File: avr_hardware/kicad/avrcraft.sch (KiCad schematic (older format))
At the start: 43 parts, among them J1 AVRISP6, P1 CONN_10, T1 S553-5999-52, U1 ATMEGA328-A_CHIPACCURATE, U2 MCP1824, U3 ENC424J600, U4 A4447SLJTR, X1 CRYSTAL, X2 25MHz

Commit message: yay added newer design
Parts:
- removed X1: CRYSTAL, XTAL4P, symbol CRYSTAL
- removed X2: 25MHz, XTAL4P, symbol CRYSTAL
- added C15: 100u, PanasonicD8Cap, symbol CAPAPOL
- added C16: .1u, SM0603, symbol C
- added P2, P3, P4, P5, P6, P7, P8: CONN_1, .1SMTPIN, symbol CONN_1
- added Q1: MOSFET_P, SOT23GDS, symbol MOSFET_P
- added X1: XTAL4P, XTAL4P, symbol XTAL4P
- added X2: 25MHz, XTAL4P, symbol XTAL4P
- D3, D4: value BRIDGE-MB2S-TP -> MB2S-TP
- D5: footprint (none) -> SM0805
- P1: value CONN_10 -> ETHERNET
- R12: value 40k -> 47k
- R13: value 1.20k -> 1k
- R14: value 6.34k -> 4.7k
- U1: value ATMEGA328-A_CHIPACCURATE -> ATMEGA328
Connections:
- net labels added: POE+B
- wire segments 235 -> 271
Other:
- note added: "NOTE: 5v Rail should be roughly 4.5V"

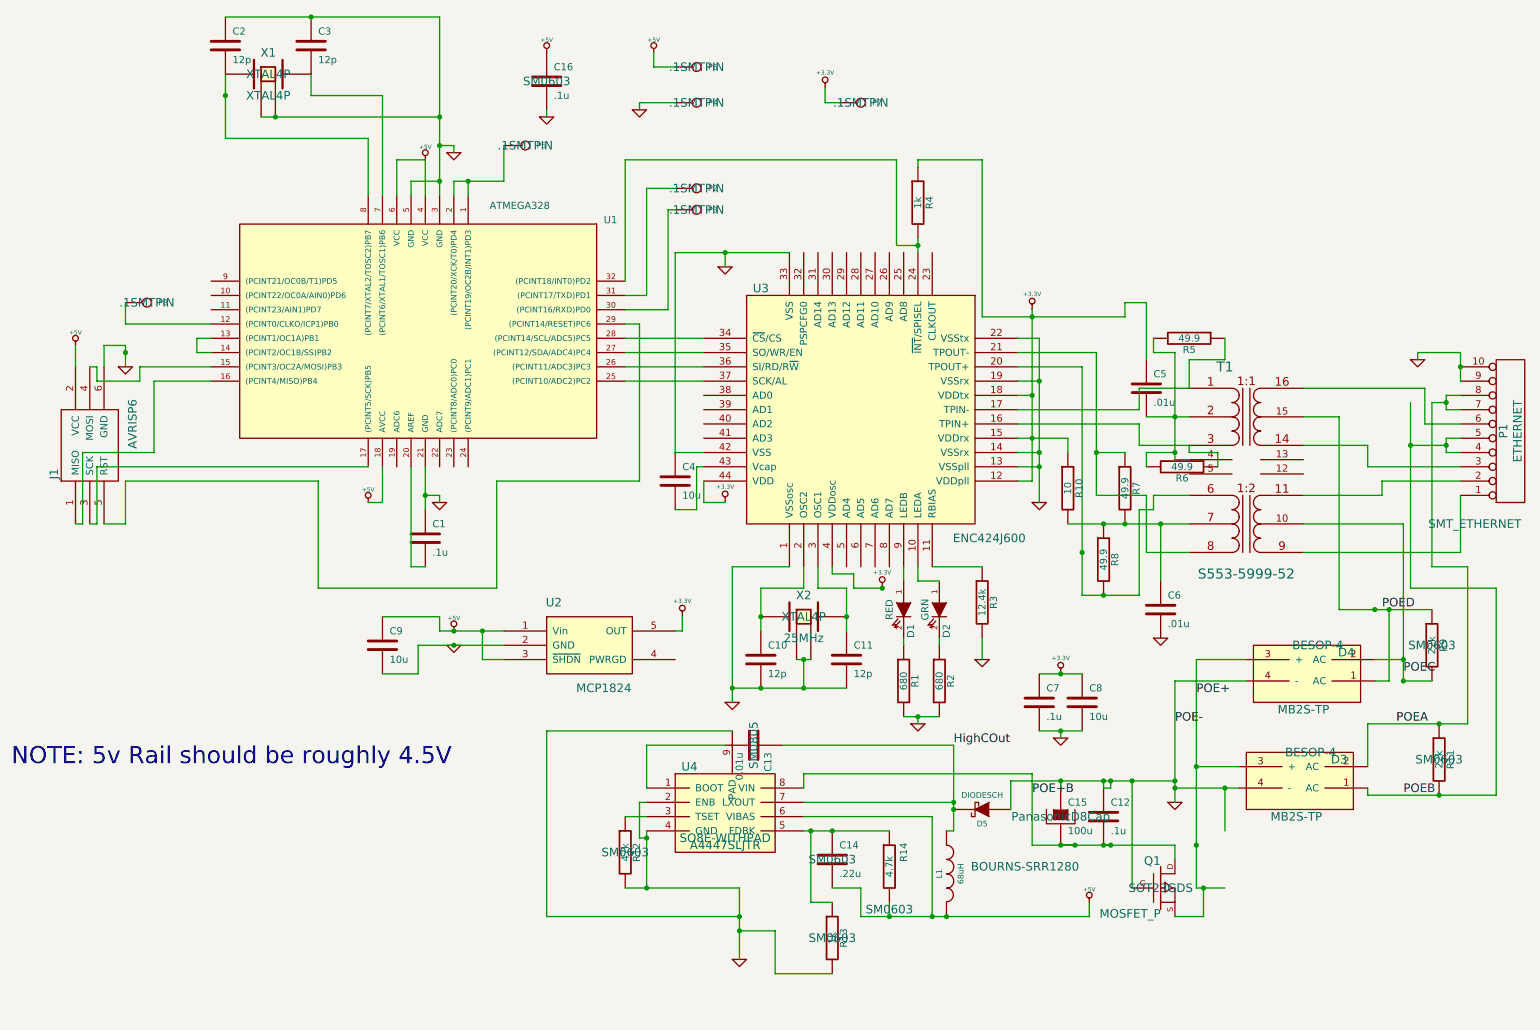
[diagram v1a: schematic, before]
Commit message: updated designs to reflect findings
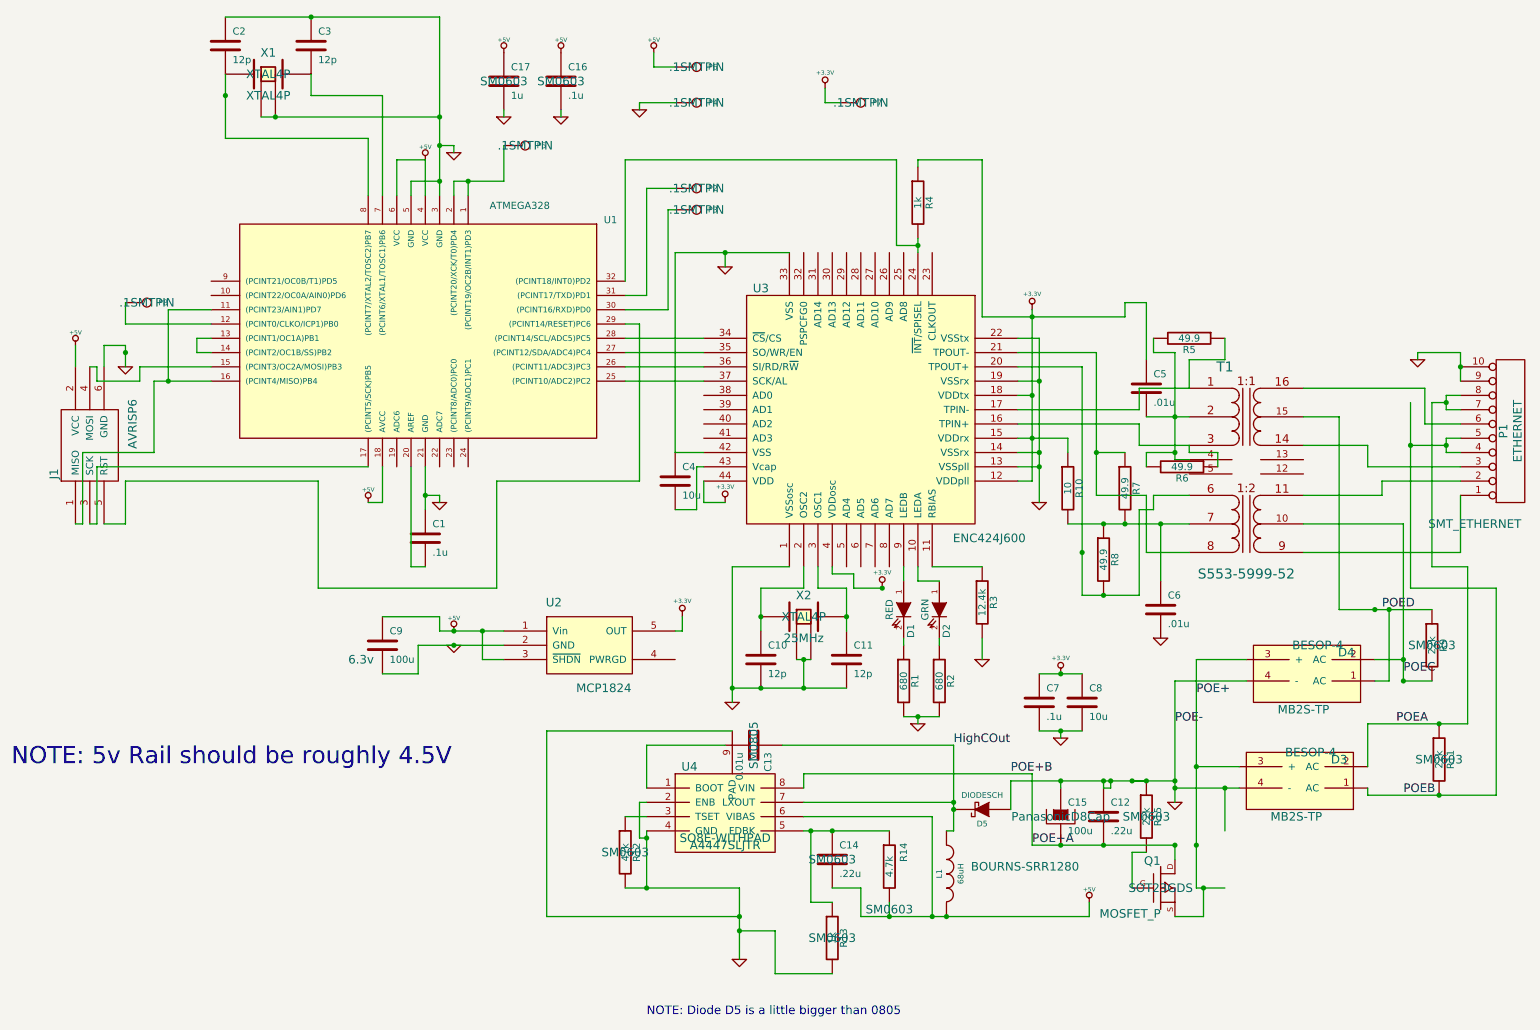
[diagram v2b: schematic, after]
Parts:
- added C17: 1u, SM0603, symbol C
- added R15: 22k, SM0603, symbol R
- C12: value .1u -> .22u
- C9: value 10u -> 100u; footprint SM0805 -> SM1206; Voltage (none) -> 6.3v
- D5: footprint SM0805 -> SM1005
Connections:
- net +5V: now also C17.1
- net GND: now also C17.2, R15.1; no longer Q1.G
- net at U1.11 ((PCINT23/AIN1)PD7): now also J1.1 (MISO), U1.16 ((PCINT4/MISO)PB4)
- net POE+B renamed POE+A
- new net: Q1.G, R15.2
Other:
- note added: "NOTE: Diode D5 is a little bigger than 0805"
- moved on the sheet: C16

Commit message: update files for actual hardware
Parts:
- added D?: ZENER, symbol ZENER
- added R16: 22k, SM0603, symbol R
- C6: footprint SM0805 -> SM0603
- R15: value 22k -> 47k
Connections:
- net GND: now also D?.1 (A); no longer R15.1
- net POE+: now also R15.1
- net at Q1.G, R15.2: now also R16.2
- new net: D?.2 (K), R16.1
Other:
- moved on the sheet: R15
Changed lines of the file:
@@
-EESchema Schematic File Version 2  date Thu 31 Jan 2013 12:07:58 AM EST
+EESchema Schematic File Version 2  date Sun 03 Feb 2013 12:44:29 AM EST
 LIBS:power
 LIBS:device
@@
 LIBS:a4447sljtr
 LIBS:crystal-4p
+LIBS:zener-sot23-3
 LIBS:avrcraft-cache
 EELAYER 25  0
@@
 Sheet 1 1
 Title ""
-Date "31 jan 2013"
+Date "3 feb 2013"
 Rev ""
 Comp ""
@@
 Comment4 ""
 $EndDescr
-Text Label 7750 6450 0    60   ~ 0
-POE+A
+Wire Wire Line
+	9900 7000 9900 7050
+Wire Wire Line
+	8750 6950 8900 6950
+Wire Wire Line
+	8900 6950 8900 5150
+Wire Wire Line
+	9900 7050 9550 7050
 Wire Wire Line
 	8750 6450 7750 6450
@@
 Connection ~ 9100 6050
 Wire Wire Line
-	9100 6350 9100 6050
+	9100 6050 9100 6350
 Connection ~ 3800 1800
 Wire Wire Line
@@
 Connection ~ 10600 6100
 Wire Wire Line
-	9250 5150 8900 5150
+	8900 5150 9250 5150
 Wire Wire Line
 	9250 5300 8750 5300
@@
 Wire Wire Line
 	1400 2800 2000 2800
-Wire Wire Line
-	8900 5150 8900 6750
-Wire Wire Line
-	8900 6750 9100 6750
 Connection ~ 8900 6450
-Wire Wire Line
-	8750 6950 8950 6950
-Wire Wire Line
-	8950 6950 8950 6750
-Connection ~ 8950 6750
 Wire Wire Line
 	7950 6050 7950 6000
@@
 Connection ~ 8750 6450
 Wire Wire Line
-	8550 6500 8450 6500
-Wire Wire Line
-	8450 6500 8450 6750
+	8900 6450 9450 6450
+Wire Wire Line
+	9100 6350 9900 6350
+Wire Wire Line
+	9900 6350 9900 6600
+Wire Wire Line
+	9050 7050 8300 7050
+Wire Wire Line
+	8300 7050 8300 6750
+Wire Wire Line
+	8300 6750 8450 6750
+Wire Wire Line
+	9450 6950 8950 6950
+Wire Wire Line
+	8950 6950 8950 7050
+Connection ~ 8950 7050
+$Comp
+L ZENER D?
+U 1 1 510DF933
+P 9900 6800
+F 0 "D?" H 9900 6900 50  0000 C CNN
+F 1 "ZENER" H 9900 6700 40  0000 C CNN
+	1    9900 6800
+	0    1    1    0
+$EndComp
+$Comp
+L R R16
+U 1 1 510DEE44
+P 9300 7050
+F 0 "R16" V 9380 7050 50  0000 C CNN
+F 1 "22k" V 9300 7050 50  0000 C CNN
+F 2 "SM0603" H 9300 7050 60  0000 C CNN
+	1    9300 7050
+	0    1    1    0
+$EndComp
+Text Label 7750 6450 0    60   ~ 0
+POE+A
 $Comp
 L R R15
 U 1 1 5109F770
-P 8550 6250
-F 0 "R15" V 8630 6250 50  0000 C CNN
-F 1 "22k" V 8550 6250 50  0000 C CNN
-F 2 "SM0603" H 8550 6250 60  0000 C CNN
-	1    8550 6250
+P 9450 6700
+F 0 "R15" V 9530 6700 50  0000 C CNN
+F 1 "47k" V 9450 6700 50  0000 C CNN
+F 2 "SM0603" H 9450 6700 60  0000 C CNN
+	1    9450 6700
 	1    0    0    -1
 $EndComp
@@
 F 0 "C6" H 8700 4900 50  0000 L CNN
 F 1 ".01u" H 8700 4700 50  0000 L CNN
-F 2 "SM0805" H 8650 4800 60  0001 C CNN
+F 2 "SM0603" H 8650 4800 60  0001 C CNN
 	1    8650 4800
 	1    0    0    -1

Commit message: oops forgot to commit this.
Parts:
- removed D?: ZENER, symbol ZENER
- added D6: ZENER-EBC3, SOT23EBC, symbol ZENER-EBC3
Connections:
- net GND: now also D6.1 (A)
- net at R16.1: now also D6.3 (K)
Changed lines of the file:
@@
-EESchema Schematic File Version 2  date Sun 03 Feb 2013 12:44:29 AM EST
+EESchema Schematic File Version 2  date Sun 03 Feb 2013 01:57:44 AM EST
 LIBS:power
 LIBS:device
@@
 Comment4 ""
 $EndDescr
+$Comp
+L ZENER-EBC3 D6
+U 1 1 510DFAA0
+P 9900 6800
+F 0 "D6" H 9900 6900 50  0000 C CNN
+F 1 "ZENER-EBC3" H 9900 6700 40  0000 C CNN
+F 2 "SOT23EBC" H 9900 6800 60  0000 C CNN
+	1    9900 6800
+	0    1    1    0
+$EndComp
 Wire Wire Line
 	9900 7000 9900 7050
@@
 Connection ~ 8950 7050
 $Comp
-L ZENER D?
-U 1 1 510DF933
-P 9900 6800
-F 0 "D?" H 9900 6900 50  0000 C CNN
-F 1 "ZENER" H 9900 6700 40  0000 C CNN
-	1    9900 6800
-	0    1    1    0
-$EndComp
-$Comp
 L R R16

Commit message: update overall design!
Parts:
- added C18, C19: 6.8n, SM0603, symbol C
- added D7: ZENER-5.6V/2W, DO214, symbol ZENER
- D6: value ZENER-EBC3 -> ZENER-20V
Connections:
- net +3.3V: no longer C5.1, R4.1
- net +5V: now also R4.1
- net GND: now also C5.2
- net POE+: now also D7.2 (K); no longer Q1.S, R15.1
- net at R4.2, U3.24 (~INT~/SPISEL): no longer U1.32 ((PCINT18/INT0)PD2)
- net at P2.1, U1.31 ((PCINT17/TXD)PD1): now also U1.32 ((PCINT18/INT0)PD2)
- net at T1.11 (S2): now also P1.1 (P1); no longer P1.2 (P2)
- net at T1.9 (S1): now also P1.2 (P2); no longer P1.1 (P1)
- new net: C18.2, R6.2, U3.16 (TPIN+)
- new net: C19.2, R5.2, U3.17 (TPIN-)
- new net: C19.1, T1.1 (RX1)
- new net: C5.1, R5.1, R6.1, T1.2 (PM)
- new net: C18.1, T1.3 (PR2)
- new net POE+C: D7.1 (A), Q1.S, R15.1
- now unconnected: T1.4 (NC)
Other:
- note added: "Connect if \nyou want\ninterrupt\nsupport"
- moved on the sheet: C5, R15, R5, R6
